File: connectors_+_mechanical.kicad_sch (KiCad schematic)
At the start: 50 parts, among them J1 Conn_01x06, J2 Conn_01x06, J3 Conn_01x04, J5 Conn_01x04, J6 Conn_01x04, Q1 BSP613P, U7 INA180A1

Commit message: started layout
Preliminary footprint selection
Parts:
- C19: footprint (none) -> Capacitor_SMD:C_0603_1608Metric_Pad1.08x0.95mm_HandSolder
- D1: footprint (none) -> Diode_SMD:D_SOD-323
- D2: footprint (none) -> Diode_SMD:D_SOD-123
- D5, D6: footprint (none) -> Diode_SMD:D_0603_1608Metric_Pad1.05x0.95mm_HandSolder
- D7: footprint (none) -> Diode_SMD:D_SMA
- F1, F2: footprint (none) -> Fuse:Fuse_1206_3216Metric
- FID1, FID2, FID3, FID4, FID5, FID6: footprint (none) -> Fiducial:Fiducial_1mm_Mask2mm
- H1: footprint (none) -> MountingHole:MountingHole_4.3mm_M4_ISO14580_Pad
- J1, J2: footprint (none) -> Connector_PinHeader_2.54mm:PinHeader_1x06_P2.54mm_Vertical_SMD_Pin1Left
- J3, J5, J6: footprint (none) -> Connector_PinHeader_2.54mm:PinHeader_1x04_P2.54mm_Vertical_SMD_Pin1Left
- Q1: footprint (none) -> Package_TO_SOT_SMD:SOT-223
- R1, R17, R18, R29, R30, R31, R42: footprint (none) -> Resistor_SMD:R_0603_1608Metric
- TP10, TP11, TP12, TP13, TP14, TP15, TP16, TP18, TP19, TP21, TP22, TP24, TP25, TP7, TP8, TP9: footprint (none) -> TestPoint:TestPoint_Pad_1.0x1.0mm
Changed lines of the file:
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@@
 			)
 		)
-		(property "Footprint" ""
+		(property "Footprint" "Fiducial:Fiducial_1mm_Mask2mm"
 			(at 242.57 57.15 0)
 			(effects
@@
 			)
 		)
-		(property "Footprint" ""
+		(property "Footprint" "TestPoint:TestPoint_Pad_1.0x1.0mm"
 			(at 39.37 73.66 0)
 			(effects
@@
 			)
 		)
-		(property "Footprint" ""
+		(property "Footprint" "TestPoint:TestPoint_Pad_1.0x1.0mm"
 			(at 49.53 73.66 0)
 			(effects
@@
 			)
 		)
-		(property "Footprint" ""
+		(property "Footprint" "Fuse:Fuse_1206_3216Metric"
 			(at 114.3 31.75 0)
 			(effects
@@
 			)
 		)
-		(property "Footprint" ""
+		(property "Footprint" "Connector_PinHeader_2.54mm:PinHeader_1x04_P2.54mm_Vertical_SMD_Pin1Left"
 			(at 157.48 35.56 0)
 			(effects
@@
 			)
 		)
-		(property "Footprint" ""
+		(property "Footprint" "Resistor_SMD:R_0603_1608Metric"
 			(at 88.9 144.78 0)
 			(effects
@@
 			)
 		)
-		(property "Footprint" ""
+		(property "Footprint" "Resistor_SMD:R_0603_1608Metric"
 			(at 132.08 129.54 0)
 			(effects
@@
 			)
 		)
-		(property "Footprint" ""
+		(property "Footprint" "TestPoint:TestPoint_Pad_1.0x1.0mm"
 			(at 49.53 29.21 0)
 			(effects
@@
 			)
 		)
-		(property "Footprint" ""
+		(property "Footprint" "Resistor_SMD:R_0603_1608Metric"
 			(at 69.85 143.51 0)
 			(effects
@@
 			)
 		)
-		(property "Footprint" ""
+		(property "Footprint" "Fiducial:Fiducial_1mm_Mask2mm"
 			(at 270.51 64.77 0)
 			(effects
@@
 			)
 		)
-		(property "Footprint" ""
+		(property "Footprint" "Resistor_SMD:R_0603_1608Metric"
 			(at 114.3 135.89 0)
 			(effects
@@
 			)
 		)
-		(property "Footprint" ""
+		(property "Footprint" "TestPoint:TestPoint_Pad_1.0x1.0mm"
 			(at 41.91 73.66 0)
 			(effects
@@
 			)
 		)
-		(property "Footprint" ""
+		(property "Footprint" "TestPoint:TestPoint_Pad_1.0x1.0mm"
 			(at 142.24 29.21 0)
 			(effects
@@
 			)
 		)
-		(property "Footprint" ""
+		(property "Footprint" "TestPoint:TestPoint_Pad_1.0x1.0mm"
 			(at 46.99 29.21 0)
 			(effects
@@
 			)
 		)
-		(property "Footprint" ""
+		(property "Footprint" "TestPoint:TestPoint_Pad_1.0x1.0mm"
 			(at 134.62 60.96 0)
 			(effects
@@
 			)
 		)
-		(property "Footprint" ""
+		(property "Footprint" "Fiducial:Fiducial_1mm_Mask2mm"
 			(at 242.57 64.77 0)
 			(effects
@@
 			)
 		)
-		(property "Footprint" ""
+		(property "Footprint" "TestPoint:TestPoint_Pad_1.0x1.0mm"
 			(at 39.37 29.21 0)
 			(effects
@@
 			)
 		)
-		(property "Footprint" ""
+		(property "Footprint" "MountingHole:MountingHole_4.3mm_M4_ISO14580_Pad"
 			(at 255.27 40.64 0)
 			(effects
@@
 			)
 		)
-		(property "Footprint" ""
+		(property "Footprint" "TestPoint:TestPoint_Pad_1.0x1.0mm"
 			(at 110.49 128.27 0)
 			(effects
@@
 			)
 		)
-		(property "Footprint" ""
+		(property "Footprint" "Connector_PinHeader_2.54mm:PinHeader_1x06_P2.54mm_Vertical_SMD_Pin1Left"
 			(at 24.13 81.28 0)
 			(effects
@@
 			)
 		)
-		(property "Footprint" ""
+		(property "Footprint" "Fiducial:Fiducial_1mm_Mask2mm"
 			(at 255.27 57.15 0)
 			(effects
@@
 			)
 		)
-		(property "Footprint" ""
+		(property "Footprint" "Connector_PinHeader_2.54mm:PinHeader_1x04_P2.54mm_Vertical_SMD_Pin1Left"
 			(at 20.32 132.08 0)
 			(effects
@@
 			)
 		)
-		(property "Footprint" ""
+		(property "Footprint" "Connector_PinHeader_2.54mm:PinHeader_1x04_P2.54mm_Vertical_SMD_Pin1Left"
 			(at 157.48 64.77 0)
 			(effects
@@
 			)
 		)
-		(property "Footprint" ""
+		(property "Footprint" "Diode_SMD:D_SOD-123"
 			(at 116.84 39.37 0)
 			(effects
@@
 			)
 		)
-		(property "Footprint" ""
+		(property "Footprint" "Connector_PinHeader_2.54mm:PinHeader_1x06_P2.54mm_Vertical_SMD_Pin1Left"
 			(at 25.4 38.1 0)
 			(effects
@@
 			)
 		)
-		(property "Footprint" ""
+		(property "Footprint" "Fuse:Fuse_1206_3216Metric"
 			(at 57.15 128.27 0)
 			(effects
@@
 			)
 		)
-		(property "Footprint" ""
+		(property "Footprint" "Resistor_SMD:R_0603_1608Metric"
 			(at 88.9 134.62 0)
 			(effects
@@
 			)
 		)
-		(property "Footprint" ""
+		(property "Footprint" "Fiducial:Fiducial_1mm_Mask2mm"
 			(at 255.27 64.77 0)
 			(effects
@@
 			)
 		)
-		(property "Footprint" ""
+		(property "Footprint" "Diode_SMD:D_0603_1608Metric_Pad1.05x0.95mm_HandSolder"
 			(at 57.15 142.24 0)
 			(effects
@@
 			)
 		)
-		(property "Footprint" ""
+		(property "Footprint" "TestPoint:TestPoint_Pad_1.0x1.0mm"
 			(at 147.32 60.96 0)
 			(effects
@@
 			)
 		)
-		(property "Footprint" ""
+		(property "Footprint" "Fiducial:Fiducial_1mm_Mask2mm"
 			(at 270.51 57.15 0)
 			(effects
@@
 			)
 		)
-		(property "Footprint" ""
+		(property "Footprint" "Diode_SMD:D_0603_1608Metric_Pad1.05x0.95mm_HandSolder"
 			(at 114.3 144.78 0)
 			(effects
@@
 			)
 		)
-		(property "Footprint" ""
+		(property "Footprint" "Resistor_SMD:R_0603_1608Metric"
 			(at 151.13 55.88 0)
 			(effects
@@
 			)
 		)
-		(property "Footprint" ""
+		(property "Footprint" "Package_TO_SOT_SMD:SOT-223"
 			(at 67.31 127 0)
 			(effects
@@
 			)
 		)
-		(property "Footprint" ""
+		(property "Footprint" "TestPoint:TestPoint_Pad_1.0x1.0mm"
 			(at 41.91 29.21 0)
 			(effects
@@
 			)
 		)
-		(property "Footprint" ""
+		(property "Footprint" "TestPoint:TestPoint_Pad_1.0x1.0mm"
 			(at 46.99 73.66 0)
 			(effects
@@
 			)
 		)
-		(property "Footprint" ""
+		(property "Footprint" "Diode_SMD:D_SOD-323"
 			(at 77.47 134.62 0)
 			(effects
@@
 			)
 		)
-		(property "Footprint" ""
+		(property "Footprint" "TestPoint:TestPoint_Pad_1.0x1.0mm"
 			(at 40.64 130.81 0)
 			(effects
@@
 			)
 		)
-		(property "Footprint" ""
+		(property "Footprint" "TestPoint:TestPoint_Pad_1.0x1.0mm"
 			(at 147.32 29.21 0)
 			(effects
@@
 			)
 		)
-		(property "Footprint" ""
+		(property "Footprint" "Resistor_SMD:R_0603_1608Metric"
 			(at 57.15 134.62 0)
 			(effects
@@
 			)
 		)
-		(property "Footprint" ""
+		(property "Footprint" "Capacitor_SMD:C_0603_1608Metric_Pad1.08x0.95mm_HandSolder"
 			(at 165.1 140.97 0)
 			(effects
@@
 			)
 		)
-		(property "Footprint" ""
+		(property "Footprint" "Diode_SMD:D_SMA"
 			(at 71.12 118.11 0)
 			(effects
@@
 			)
 		)
-		(property "Footprint" ""
+		(property "Footprint" "TestPoint:TestPoint_Pad_1.0x1.0mm"
 			(at 152.4 60.96 0)
 			(effects
@@
 			)
 		)
-		(property "Footprint" ""
+		(property "Footprint" "TestPoint:TestPoint_Pad_1.0x1.0mm"
 			(at 140.97 60.96 0)
 			(effects

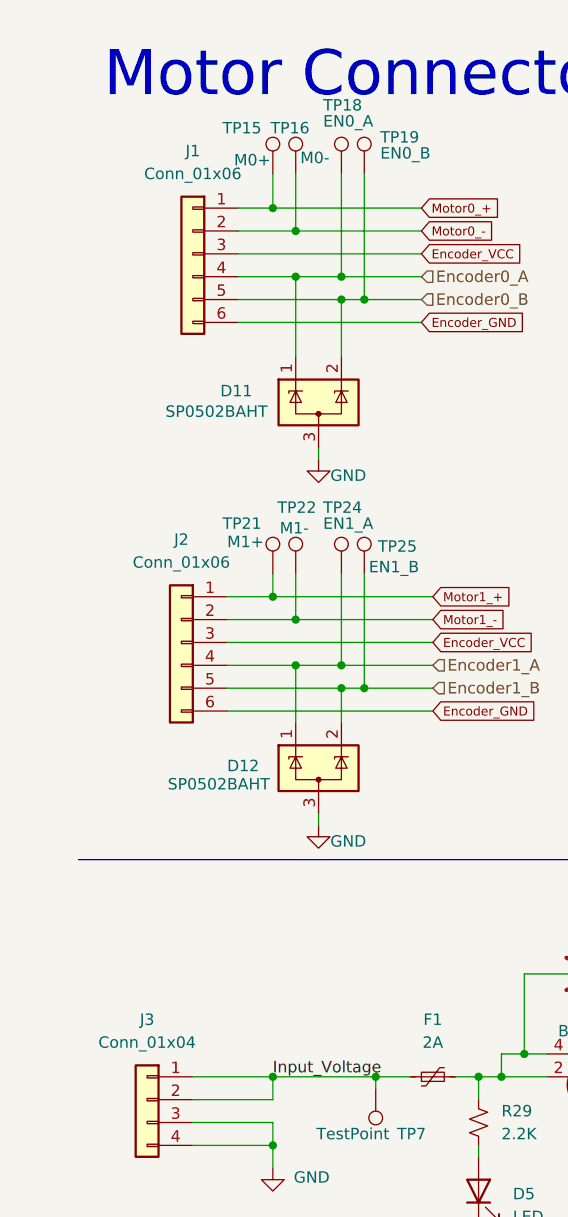
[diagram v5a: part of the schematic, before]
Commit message: footprint cleanup
switched to 0402 resistors, updated connectors, etc...
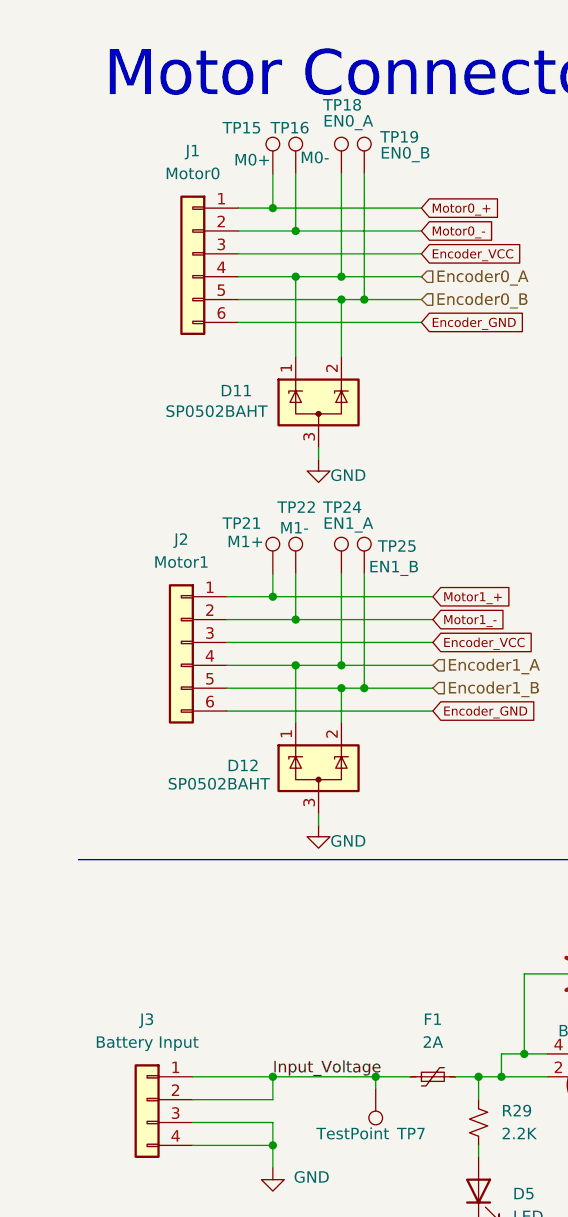
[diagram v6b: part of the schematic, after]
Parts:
- J1: value Conn_01x06 -> Motor0; footprint Connector_PinHeader_2.54mm:PinHeader_1x06_P2.54mm_Vertical_SMD_Pin1Left -> Connector_JST:JST_SH_SM06B-SRSS-TB_1x06-1MP_P1.00mm_Horizontal
- J2: value Conn_01x06 -> Motor1; footprint Connector_PinHeader_2.54mm:PinHeader_1x06_P2.54mm_Vertical_SMD_Pin1Left -> Connector_JST:JST_SH_SM06B-SRSS-TB_1x06-1MP_P1.00mm_Horizontal
- J3: value Conn_01x04 -> Battery Input; footprint Connector_PinHeader_2.54mm:PinHeader_1x04_P2.54mm_Vertical_SMD_Pin1Left -> Connector_JST:JST_SH_BM04B-SRSS-TB_1x04-1MP_P1.00mm_Vertical
- J5, J6: footprint Connector_PinHeader_2.54mm:PinHeader_1x04_P2.54mm_Vertical_SMD_Pin1Left -> Connector_PinHeader_2.54mm:PinHeader_1x04_P2.54mm_Vertical
- R1, R17, R18, R29, R30, R31, R42: footprint Resistor_SMD:R_0603_1608Metric -> Resistor_SMD:R_0402_1005Metric
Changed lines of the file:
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@@
 			)
 		)
-		(property "Footprint" "Connector_PinHeader_2.54mm:PinHeader_1x04_P2.54mm_Vertical_SMD_Pin1Left"
+		(property "Footprint" "Connector_PinHeader_2.54mm:PinHeader_1x04_P2.54mm_Vertical"
 			(at 157.48 35.56 0)
 			(effects
@@
 			)
 		)
-		(property "Footprint" "Resistor_SMD:R_0603_1608Metric"
+		(property "Footprint" "Resistor_SMD:R_0402_1005Metric"
 			(at 88.9 144.78 0)
 			(effects
@@
 			)
 		)
-		(property "Footprint" "Resistor_SMD:R_0603_1608Metric"
+		(property "Footprint" "Resistor_SMD:R_0402_1005Metric"
 			(at 132.08 129.54 0)
 			(effects
@@
 			)
 		)
-		(property "Footprint" "Resistor_SMD:R_0603_1608Metric"
+		(property "Footprint" "Resistor_SMD:R_0402_1005Metric"
 			(at 69.85 143.51 0)
 			(effects
@@
 			)
 		)
-		(property "Footprint" "Resistor_SMD:R_0603_1608Metric"
+		(property "Footprint" "Resistor_SMD:R_0402_1005Metric"
 			(at 114.3 135.89 0)
 			(effects
@@
 			)
 		)
-		(property "Value" "Conn_01x06"
+		(property "Value" "Motor1"
 			(at 24.13 72.39 0)
 			(effects
@@
 			)
 		)
-		(property "Footprint" "Connector_PinHeader_2.54mm:PinHeader_1x06_P2.54mm_Vertical_SMD_Pin1Left"
+		(property "Footprint" "Connector_JST:JST_SH_SM06B-SRSS-TB_1x06-1MP_P1.00mm_Horizontal"
 			(at 24.13 81.28 0)
 			(effects
@@
 			)
 		)
-		(property "Value" "Conn_01x04"
+		(property "Value" "Battery Input"
 			(at 20.32 125.73 0)
 			(effects
@@
 			)
 		)
-		(property "Footprint" "Connector_PinHeader_2.54mm:PinHeader_1x04_P2.54mm_Vertical_SMD_Pin1Left"
+		(property "Footprint" "Connector_JST:JST_SH_BM04B-SRSS-TB_1x04-1MP_P1.00mm_Vertical"
 			(at 20.32 132.08 0)
 			(effects
@@
 			)
 		)
-		(property "Footprint" "Connector_PinHeader_2.54mm:PinHeader_1x04_P2.54mm_Vertical_SMD_Pin1Left"
+		(property "Footprint" "Connector_PinHeader_2.54mm:PinHeader_1x04_P2.54mm_Vertical"
 			(at 157.48 64.77 0)
 			(effects
@@
 			)
 		)
-		(property "Value" "Conn_01x06"
+		(property "Value" "Motor0"
 			(at 25.4 29.21 0)
 			(effects
@@
 			)
 		)
-		(property "Footprint" "Connector_PinHeader_2.54mm:PinHeader_1x06_P2.54mm_Vertical_SMD_Pin1Left"
+		(property "Footprint" "Connector_JST:JST_SH_SM06B-SRSS-TB_1x06-1MP_P1.00mm_Horizontal"
 			(at 25.4 38.1 0)
 			(effects
@@
 			)
 		)
-		(property "Footprint" "Resistor_SMD:R_0603_1608Metric"
+		(property "Footprint" "Resistor_SMD:R_0402_1005Metric"
 			(at 88.9 134.62 0)
 			(effects
@@
 			)
 		)
-		(property "Footprint" "Resistor_SMD:R_0603_1608Metric"
+		(property "Footprint" "Resistor_SMD:R_0402_1005Metric"
 			(at 151.13 55.88 0)
 			(effects
@@
 			)
 		)
-		(property "Footprint" "Resistor_SMD:R_0603_1608Metric"
+		(property "Footprint" "Resistor_SMD:R_0402_1005Metric"
 			(at 57.15 134.62 0)
 			(effects

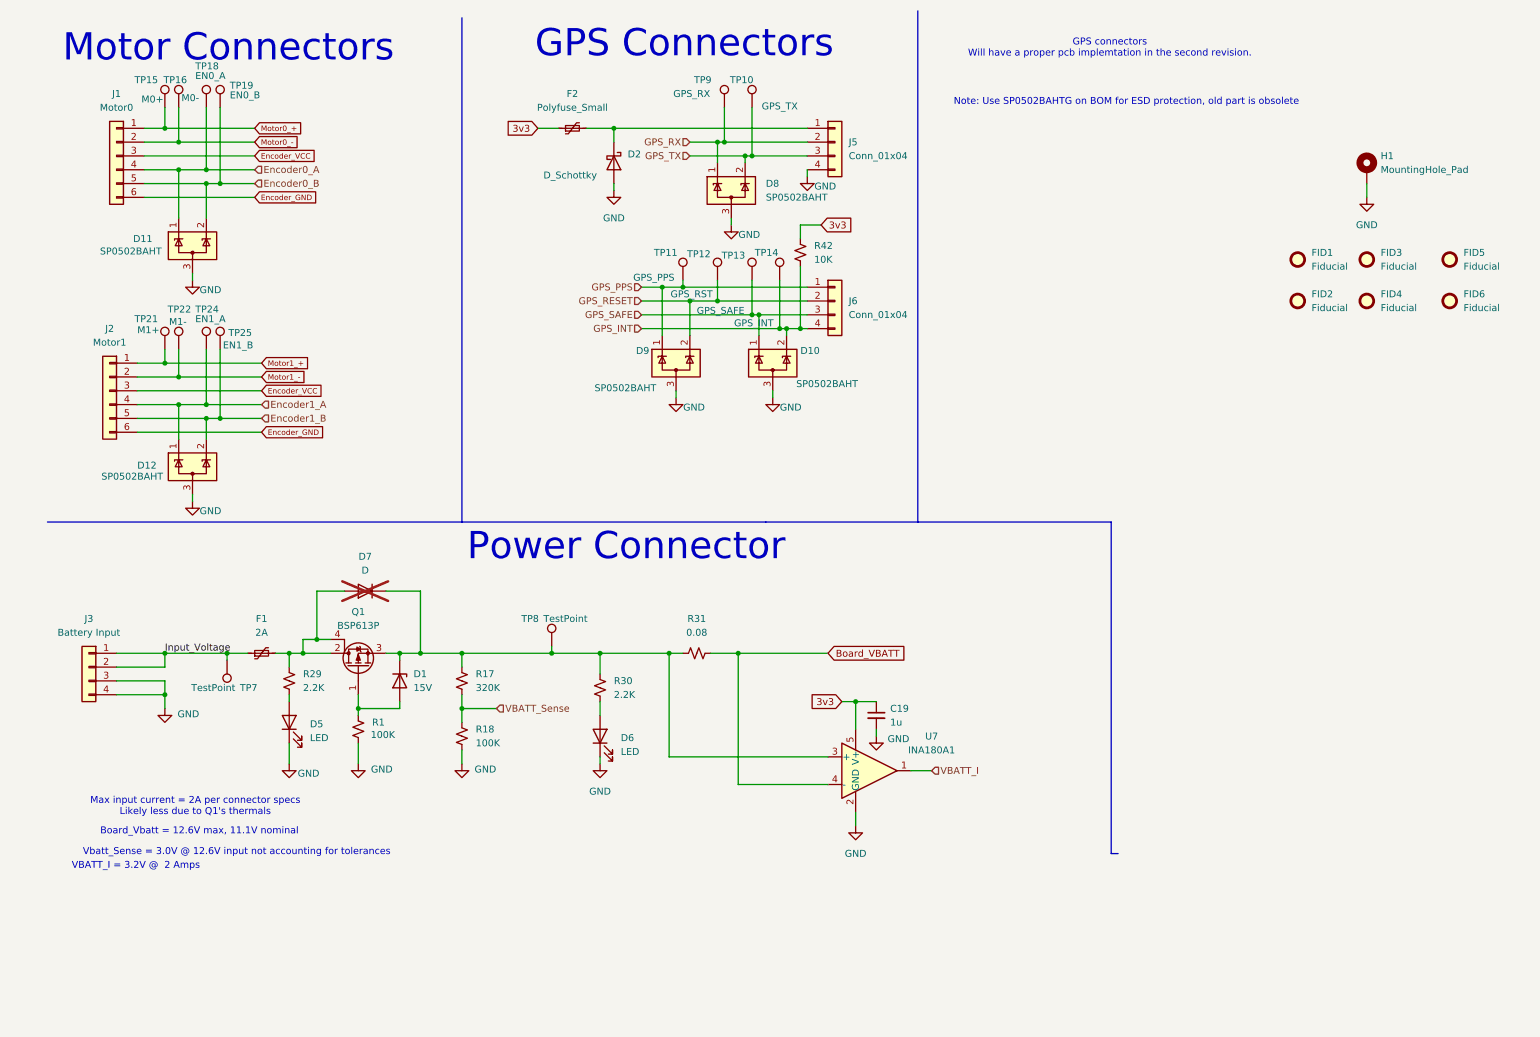
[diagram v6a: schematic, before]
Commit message: Added USB C Connector
Added usb C connector, consolidated ESD parts, cleaned up footprint selection.
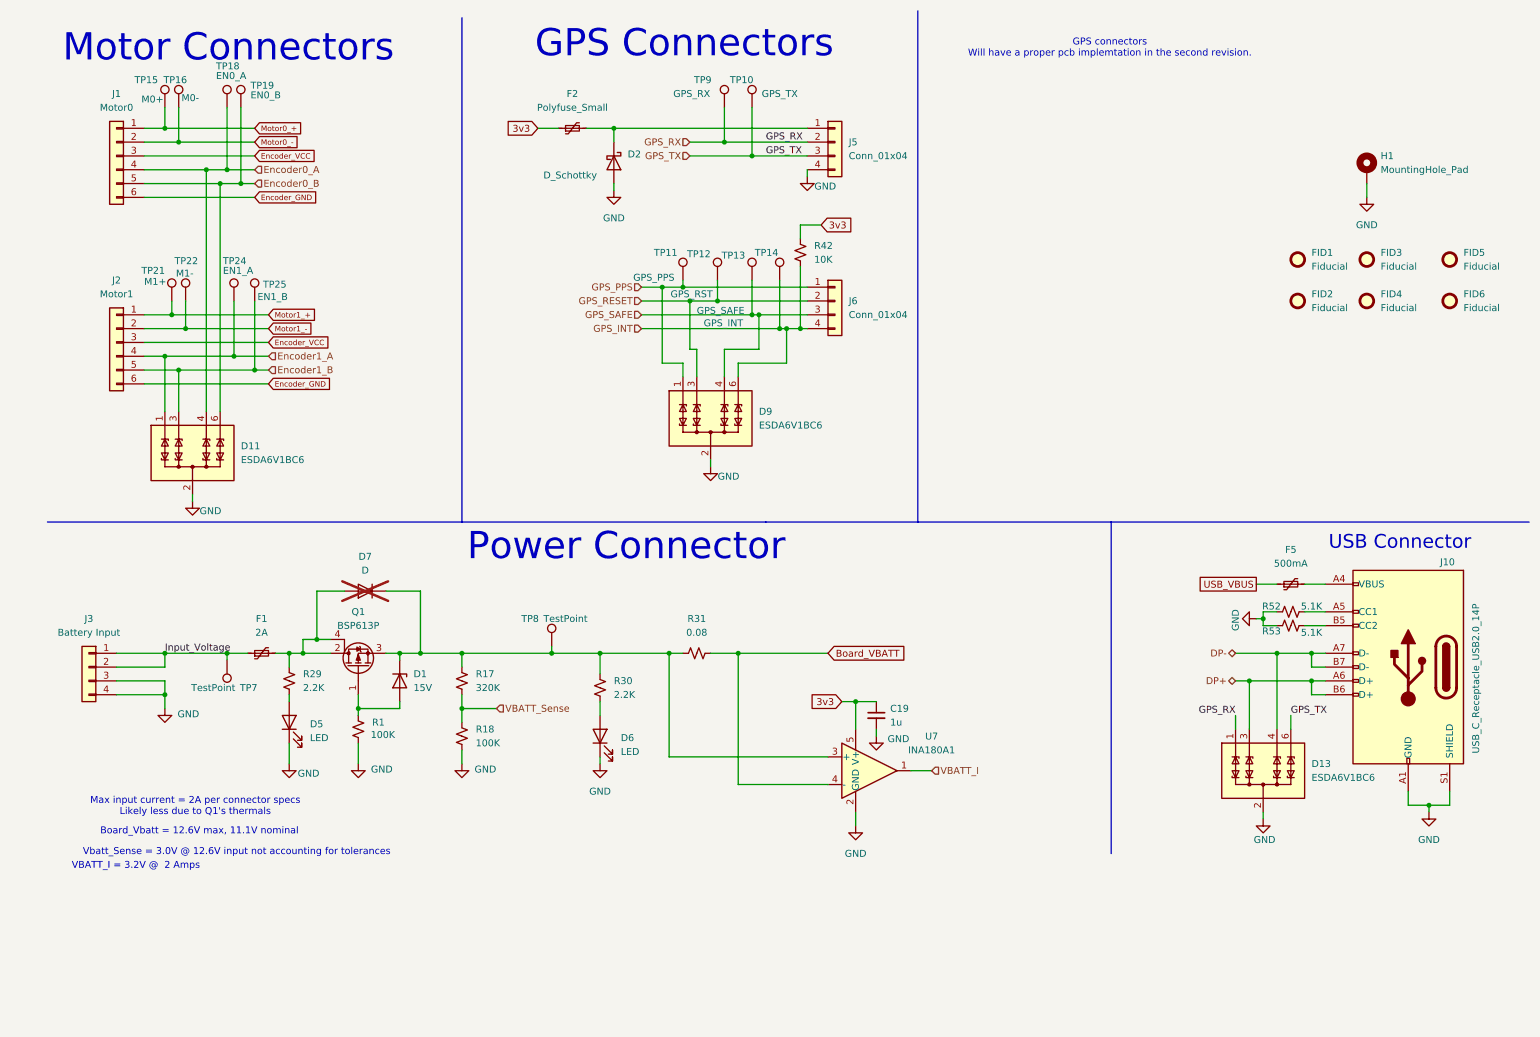
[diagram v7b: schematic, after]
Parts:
- removed D10, D11, D12, D8, D9: SP0502BAHT, Package_TO_SOT_SMD:SOT-23, symbol Power_Protection:SP0502BAHT
- added D11, D13, D9: ESDA6V1BC6, Package_TO_SOT_SMD:SOT-23-6, symbol Power_Protection:ESDA6V1BC6
- added F5: 500mA, Fuse:Fuse_1206_3216Metric, symbol Device:Polyfuse_Small
- added J10: USB_C_Receptacle_USB2.0_14P, Connector_USB:USB_C_Receptacle_Amphenol_12401610E4-2A_CircularHoles, symbol Connector:USB_C_Receptacle_USB2.0_14P
- added R52, R53: 5.1K, Resistor_SMD:R_0402_1005Metric, symbol Device:R_Small_US
- J1, J2: footprint Connector_JST:JST_SH_SM06B-SRSS-TB_1x06-1MP_P1.00mm_Horizontal -> Connector_JST:JST_SH_BM06B-SRSS-TB_1x06-1MP_P1.00mm_Vertical
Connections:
- net Encoder0_A: now also D11.4 (TVS3)
- net Encoder0_B: now also D11.6 (TVS4)
- net Encoder1_A: now also D11.1 (TVS1)
- net Encoder1_B: now also D11.3 (TVS2)
- net GND: now also D11.2 (COM), D11.5 (COM), D13.2 (COM), D13.5 (COM), D9.2 (COM), D9.5 (COM), J10.A1 (GND), J10.A12 (GND), J10.B1 (GND), J10.B12 (GND), J10.S1 (SHIELD), R52.1, R53.1
- net GPS_INT: now also D9.6 (TVS4)
- net GPS_PPS: now also D9.1 (TVS1)
- net GPS_RESET: now also D9.3 (TVS2)
- net GPS_RX: now also D13.1 (TVS1)
- net GPS_SAFE: now also D9.4 (TVS3)
- net GPS_TX: now also D13.6 (TVS4)
- new net: F5.2, J10.A4 (VBUS), J10.A9 (VBUS), J10.B4 (VBUS), J10.B9 (VBUS)
- new net: J10.A5 (CC1), R52.2
- new net: J10.B5 (CC2), R53.2
- new net DP+: D13.3 (TVS2), J10.A6 (D+), J10.B6 (D+)
- new net DP-: D13.4 (TVS3), J10.A7 (D-), J10.B7 (D-)
- new net USB_VBUS: F5.1
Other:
- note added: "USB Connector"
- note removed: "Note: Use SP0502BAHTG on BOM for ESD protection, old part is obsolete"
- moved on the sheet: J2, TP18, TP19, TP21, TP22, TP24, TP25

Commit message: Swapped USB to Vert
Changed USB-C connector from horizontal to vertical
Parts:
- J10: footprint Connector_USB:USB_C_Receptacle_Amphenol_12401610E4-2A_CircularHoles -> GCT:GCT_USB4115-03-C_REVB4
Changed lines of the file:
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@@
 			)
 		)
-		(property "Footprint" "Connector_USB:USB_C_Receptacle_Amphenol_12401610E4-2A_CircularHoles"
+		(property "Footprint" "GCT:GCT_USB4115-03-C_REVB4"
 			(at 259.08 132.08 0)
 			(effects
